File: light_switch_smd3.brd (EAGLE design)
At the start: 45.7 x 45.7 mm, 26 parts, among them U1 ESP8266_ESP-01

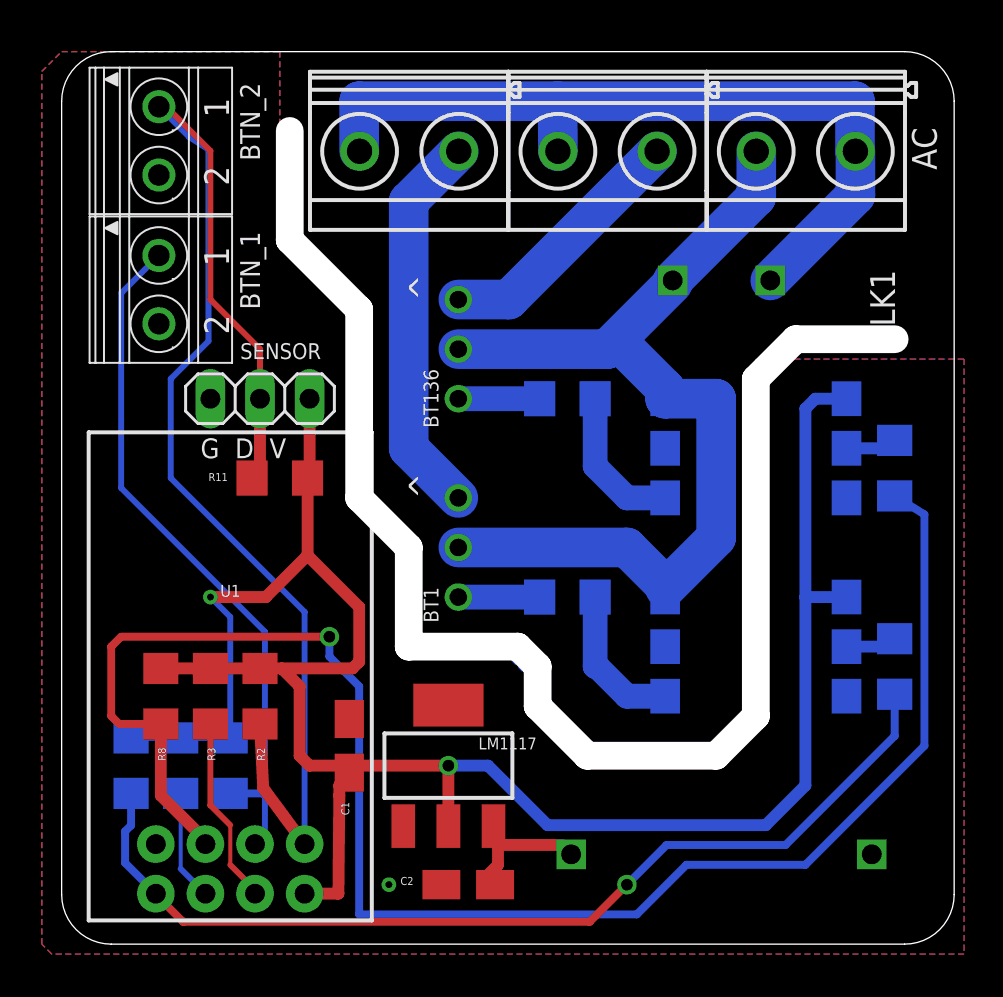
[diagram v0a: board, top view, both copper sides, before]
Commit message: added LEDs, more rounded corners, +5V power connector
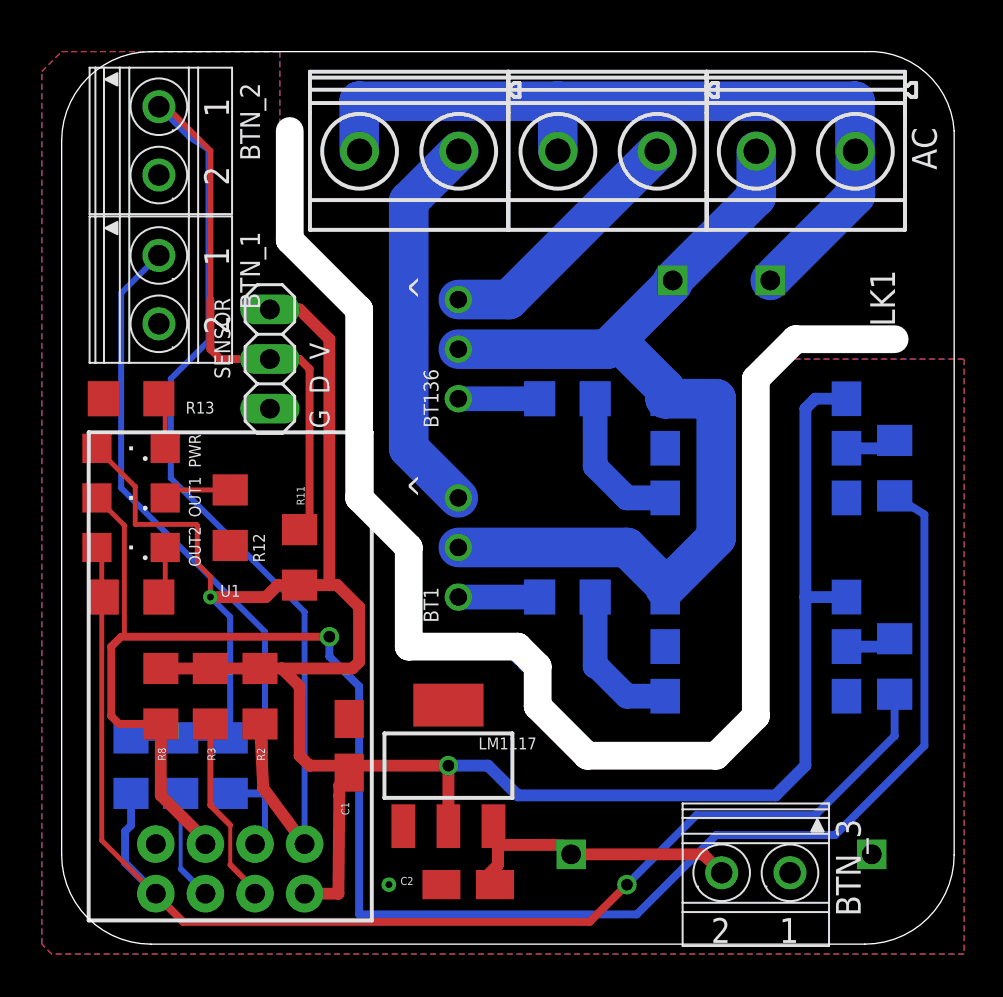
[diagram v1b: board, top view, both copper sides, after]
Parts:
- added BTN_3: 1751248, con-phoenix-350:1751248
- added OUT1, OUT2, PWR: (no value), led:SML1206
- added R12, R13, R14: 3.3K, resistor:R1206
- moved R11 4.19 mm to (12.2, 19.8), turned to 90 degrees
- moved SENSOR 2.09 mm to (10.7, 30.0), turned to 90 degrees
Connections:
- new net N$1: PWR.C, R13.2
- new net N$11: OUT2.C, R14.2
- new net N$9: OUT1.C, R12.2
- net +3V3: now also PWR.A
- net +5V: now also BTN_3.2
- net GND: now also BTN_3.1, R12.1, R13.1, R14.1
- net GPIO2: now also OUT1.A
- net TXD: now also OUT2.A
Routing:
- net TXD: track 50.5 -> 69.5 mm
- net +3V3: track 112.9 -> 129.9 mm
- net +5V: track 7.60 -> 15.7 mm
- net GPIO2: track 85.8 -> 93.3 mm
- net RXD: track 71.1 -> 77.4 mm
- net N$9: track 0.00 -> 3.50 mm
- net N$1: track 0.00 -> 2.68 mm
- net N$11: track 0.00 -> 2.68 mm
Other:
- outline, holes or cut-outs redrawn

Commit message: added pcf8574 due to undefined state of GPIOs during boot
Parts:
- removed R2: 3.3K, resistor:R1206
- added IC1: PCF8574T, micro-philips:SO16W
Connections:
- new net P0: BTN_1.1, IC1.4
- new net P1: BTN_2.1, IC1.5
- new net P2: IC1.6, OUT1.C, R6.1
- new net P3: IC1.7, OUT2.C, R9.1
- net +3V3: now also IC1.16, R12.2, R14.2; no longer R2.2
- net GND: now also IC1.1, IC1.2, IC1.3, IC1.8; no longer R12.1, R14.1
- net GPIO0: now also IC1.15; no longer BTN_1.1
- net GPIO2: now also IC1.14; no longer OUT1.A, R6.1
- net N$11: now also OUT2.A, R14.1; no longer OUT2.C, R14.2
- net N$9: now also OUT1.A, R12.1; no longer OUT1.C, R12.2
- net RXD: no longer BTN_2.1, R2.1, U1.5
- net TXD: no longer OUT2.A, R9.1
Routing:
- net GPIO2: track 93.3 -> 21.4 mm, vias 1 -> 0
- net RXD: track 77.4 -> 9.62 mm
- net TXD: track 69.5 -> 5.96 mm, vias 1 -> 0
- net P2: track 0.00 -> 59.3 mm
- net P3: track 0.00 -> 59.1 mm, vias 0 -> 1
- net P1: track 0.00 -> 20.9 mm
- net GPIO0: track 36.0 -> 17.9 mm
- net P0: track 0.00 -> 12.7 mm
- net N$9: track 3.50 -> 7.84 mm
- net +3V3: track 129.9 -> 133.5 mm

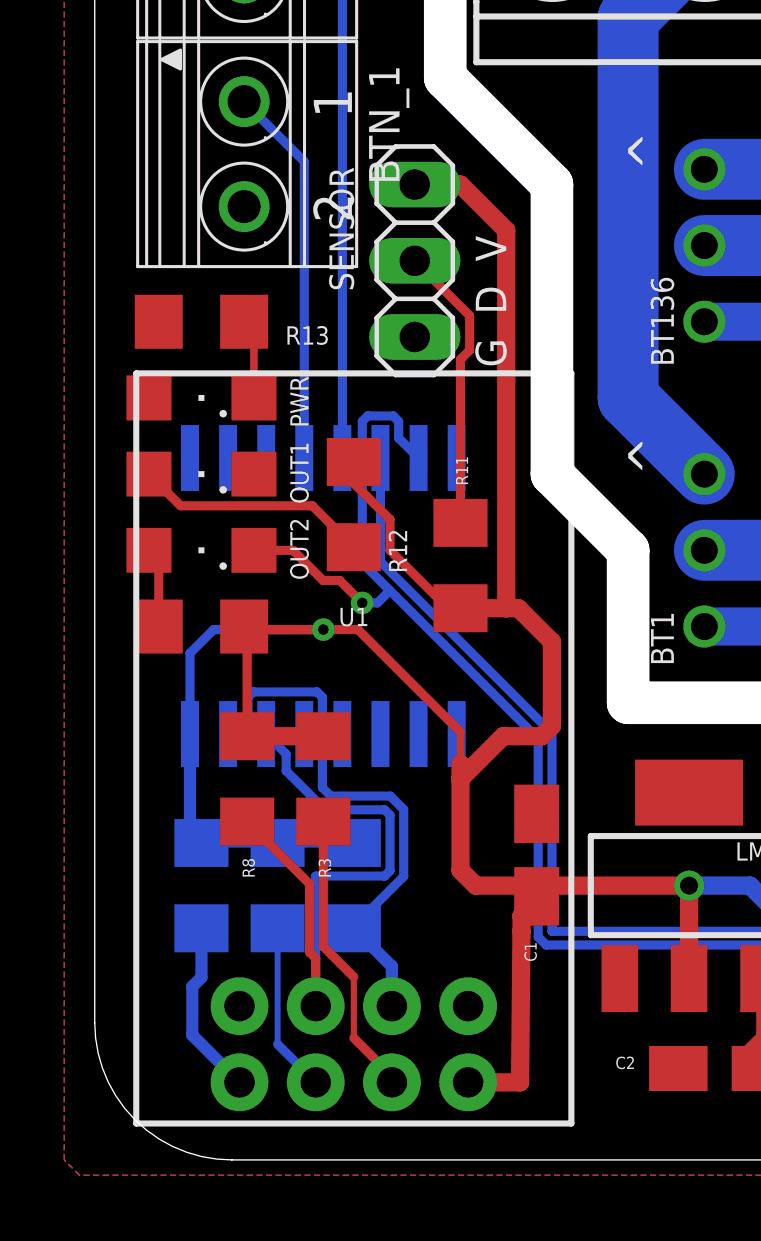
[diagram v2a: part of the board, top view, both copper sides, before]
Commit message: DRC checked, no airwires
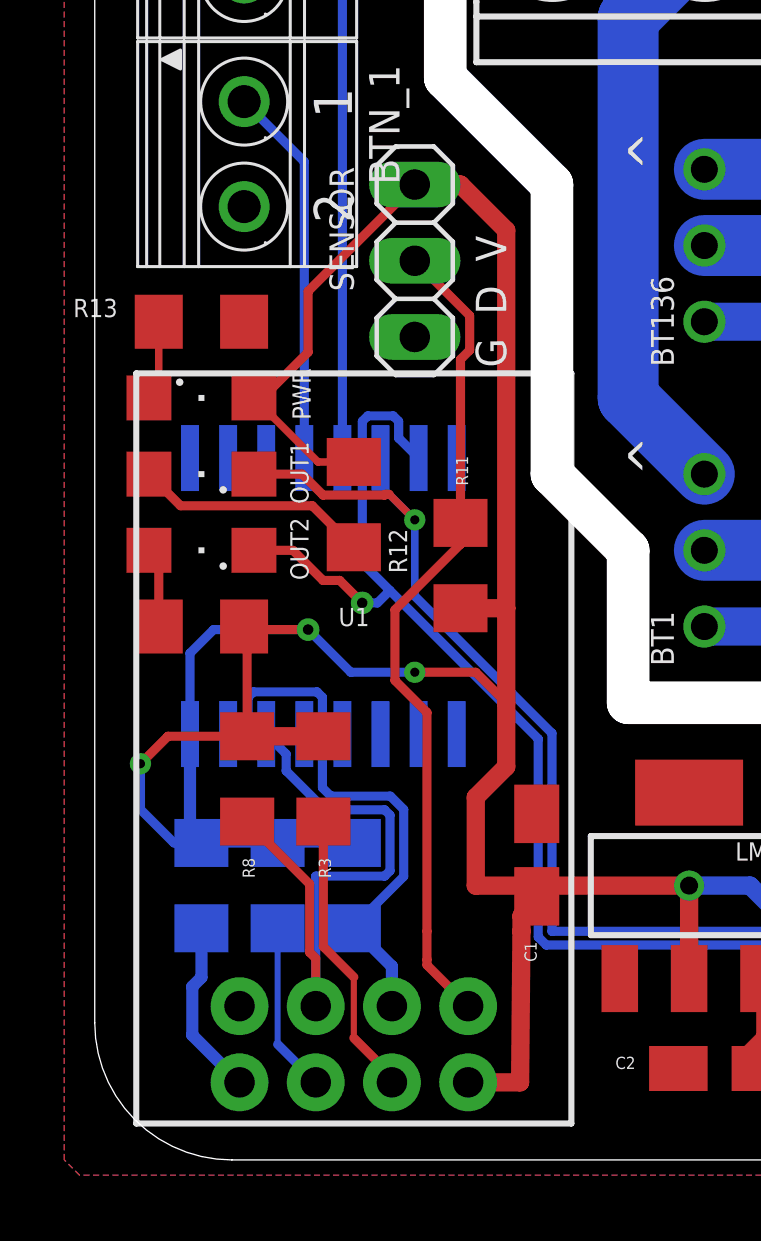
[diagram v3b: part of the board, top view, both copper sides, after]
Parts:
- turned PWR to 0 degrees
- turned R13 to 180 degrees
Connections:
- net RXD: now also U1.5
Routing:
- net RXD: track 9.62 -> 27.6 mm
- net +3V3: track 133.5 -> 142.4 mm, vias 2 -> 4
- net P2: track 59.3 -> 65.3 mm, vias 0 -> 1

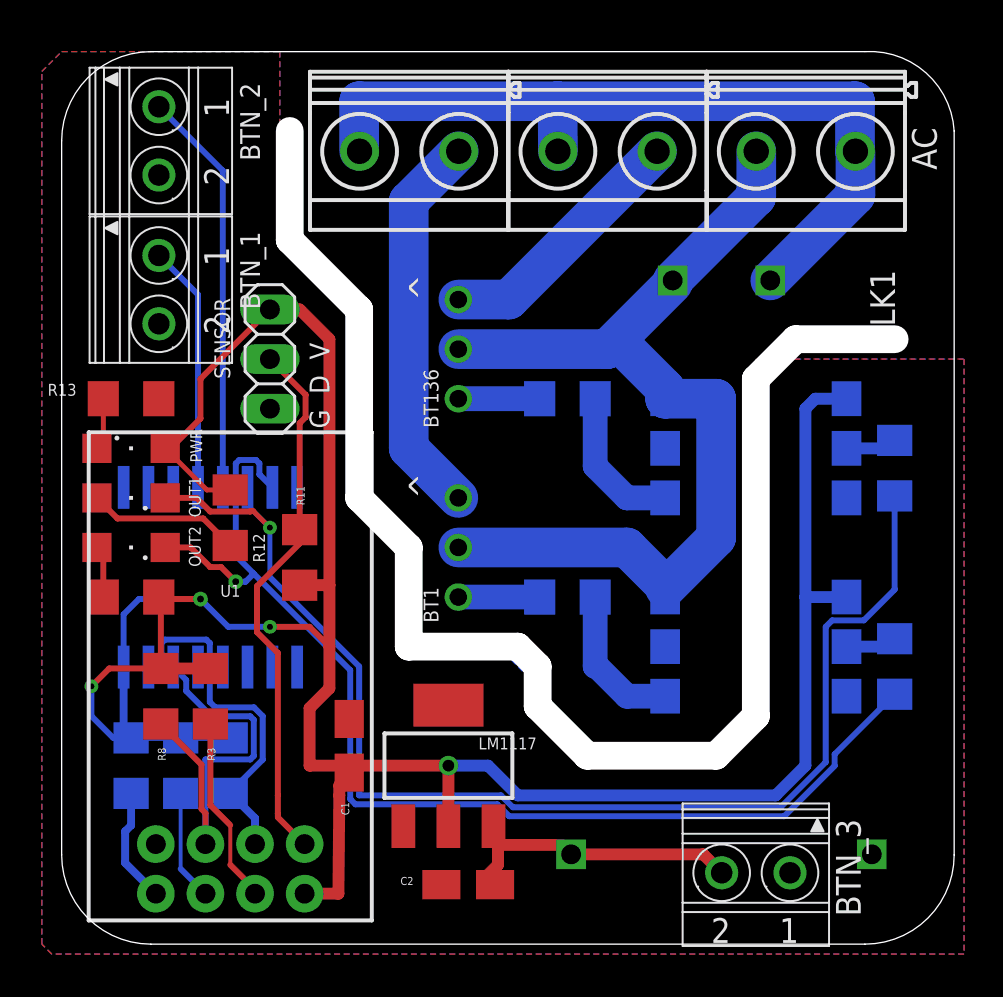
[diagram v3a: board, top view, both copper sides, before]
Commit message: added pinheader and small fixes
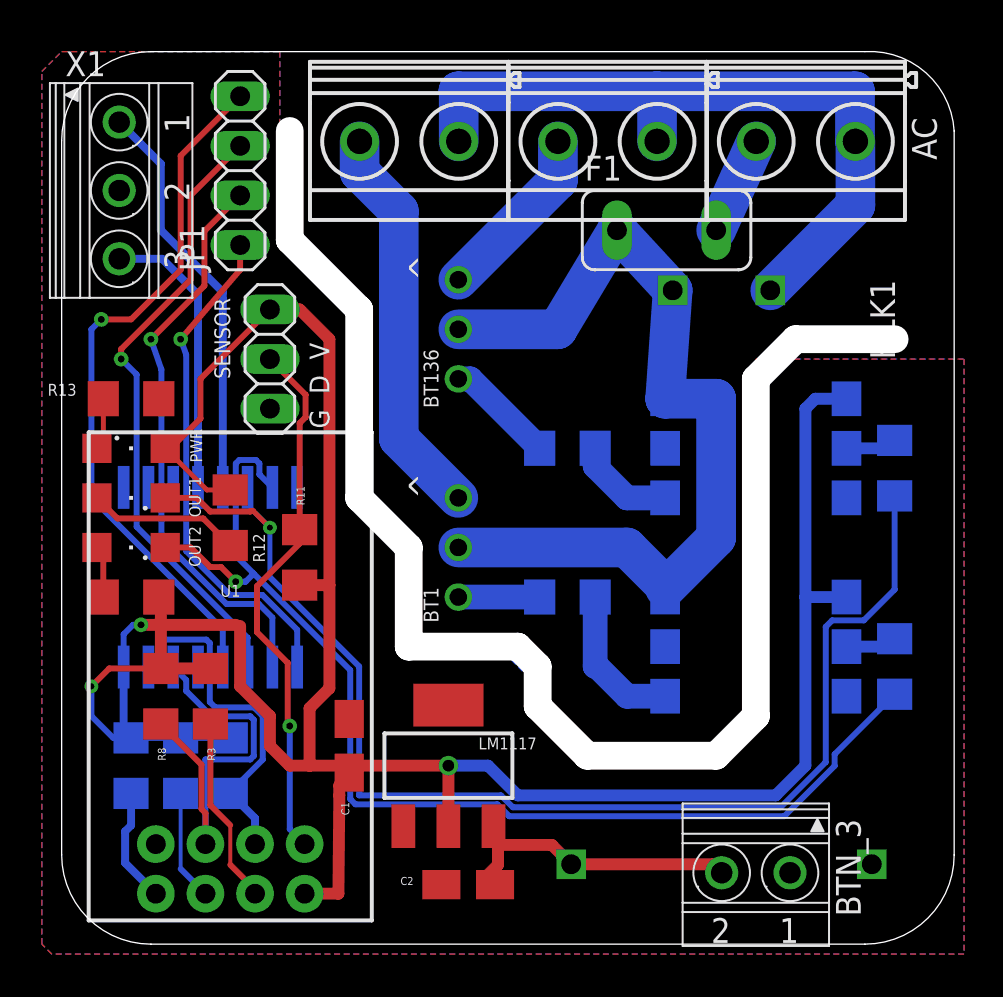
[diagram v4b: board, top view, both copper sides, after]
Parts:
- removed BTN_1, BTN_2: 1751248, con-phoenix-350:1751248
- added F1: (no value), fuse:TE5
- added JP1: (no value), pinhead:1X04
- added X1: 1751251, con-phoenix-350:1751251
- moved R7 2.54 mm to (25.9, 25.4)
- moved BT136 1.02 mm to (20.3, 31.5)
- moved AC 0.51 mm to (38.1, 41.1)
- moved OUT_1 0.51 mm to (27.9, 41.1)
- moved OUT_2 0.51 mm to (17.8, 41.1)
- moved HLK1 0.51 mm to (33.8, 18.8)
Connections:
- new net P4: IC1.9, JP1.1
- new net P5: IC1.10, JP1.2
- new net P6: IC1.11, JP1.3
- new net P7: IC1.12, JP1.4
- new net V230FUSE: BT1.T2, BT136.T2, F1.1, HLK1.P$2, OK1.6, OK2.6
- net GND: now also X1.2; no longer BTN_1.2, BTN_2.2
- net N$4: now also OUT_1.2; no longer OUT_1.1
- net N$8: now also OUT_2.2; no longer OUT_2.1
- net P0: now also X1.3; no longer BTN_1.1
- net P1: now also X1.1; no longer BTN_2.1
- net VPP: now also F1.2; no longer BT1.T2, BT136.T2, HLK1.P$2, OK1.6, OK2.6
- net VSS: now also OUT_1.1, OUT_2.1; no longer OUT_1.2, OUT_2.2
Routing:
- net V230FUSE: track 0.00 -> 46.6 mm
- net VPP: track 51.1 -> 4.99 mm
- net P7: track 0.00 -> 36.1 mm, vias 0 -> 1
- net P6: track 0.00 -> 31.9 mm, vias 0 -> 1
- net P5: track 0.00 -> 29.5 mm, vias 0 -> 1
- net P4: track 0.00 -> 26.1 mm, vias 0 -> 1
- net N$4: track 13.3 -> 9.20 mm
- net VSS: track 41.5 -> 37.5 mm
- net N$7: track 7.71 -> 5.17 mm
- net P0: track 12.7 -> 14.7 mm
- net N$6: track 4.17 -> 5.64 mm
- net +3V3: track 142.4 -> 142.8 mm, vias 4 -> 3
- net RXD: vias 0 -> 1

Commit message: descriptions adjusted
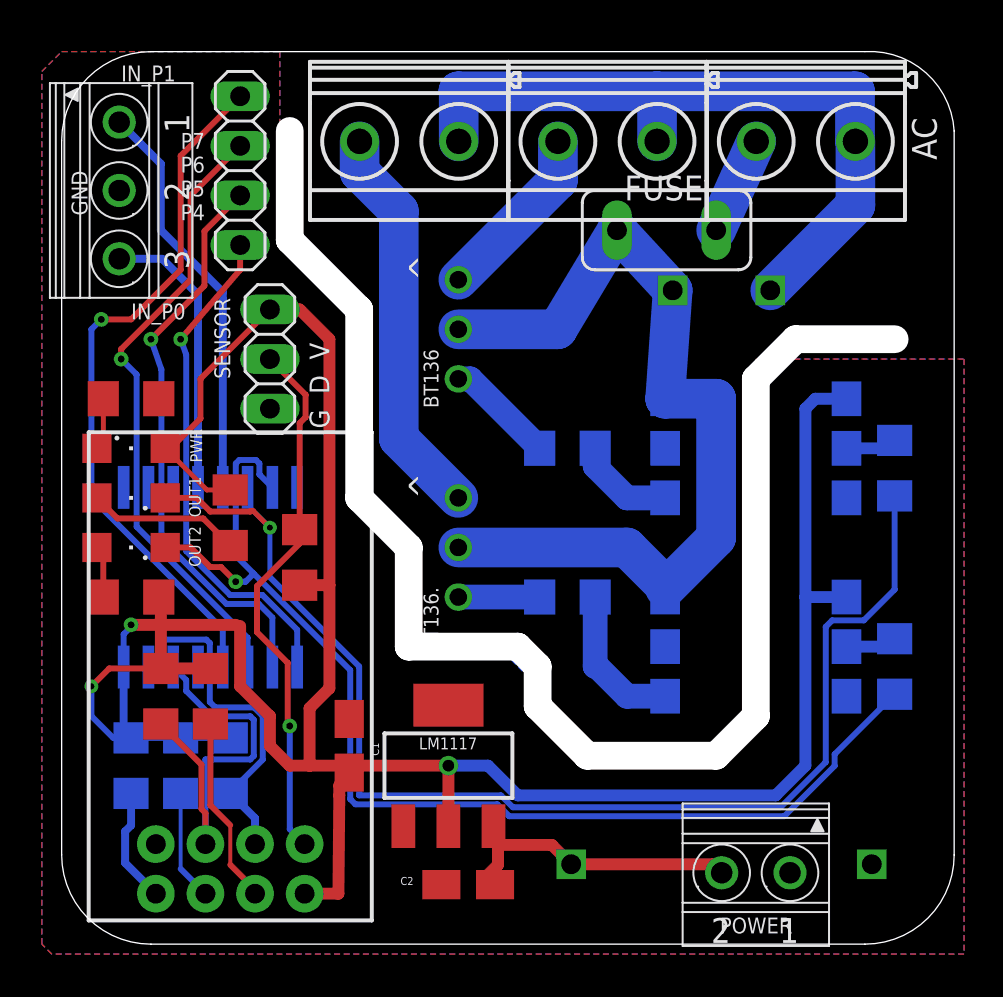
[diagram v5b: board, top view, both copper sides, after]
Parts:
- renumbered BT1 to BT136., BTN_3 to POWER, F1 to FUSE, OUT_1 to OUT_P2, OUT_2 to OUT_P3
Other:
- board text added: "5V"
- board text added: "GND"
- board text added: "IN_P0"
- board text added: "IN_P1"
- board text added: "P7 P6 P5 P4"
